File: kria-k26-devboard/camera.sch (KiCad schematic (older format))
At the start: 9 parts, among them J3 WE_68715014522, U9 PI4MSD5V9540BUEX

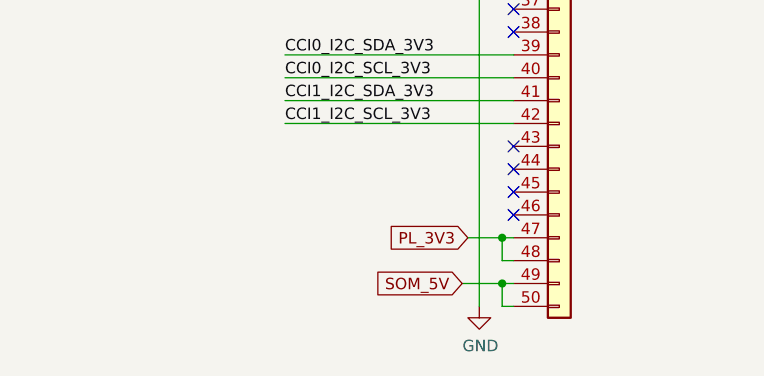
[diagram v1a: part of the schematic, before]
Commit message: Finished Power planes and overall connectivity
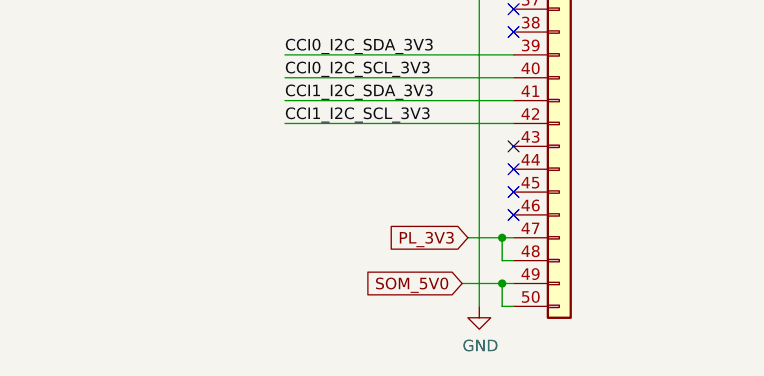
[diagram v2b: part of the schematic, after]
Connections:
- net SOM_5V renamed SOM_5V0
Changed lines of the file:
@@
 NoConn ~ 8500 5100
 Text GLabel 8275 5700 0    50   Input ~ 0
-SOM_5V
+SOM_5V0
 Wire Wire Line
 	8500 5800 8450 5800

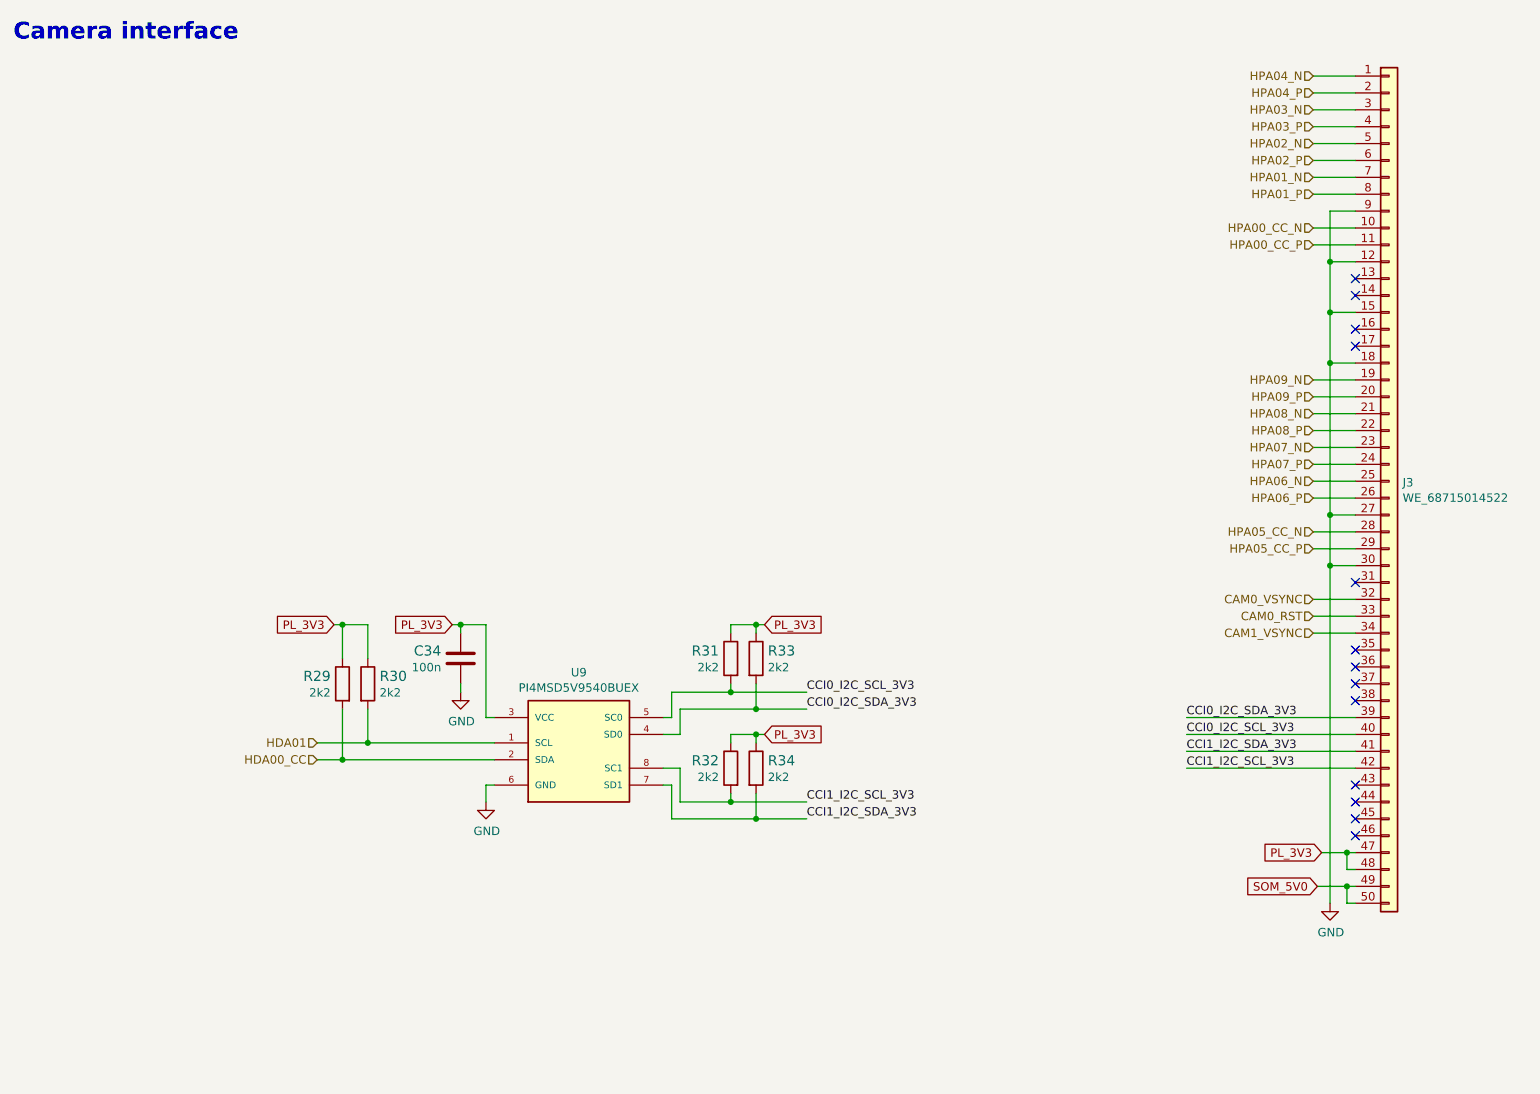
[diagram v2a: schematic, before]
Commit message: Applied schematic review suggestions
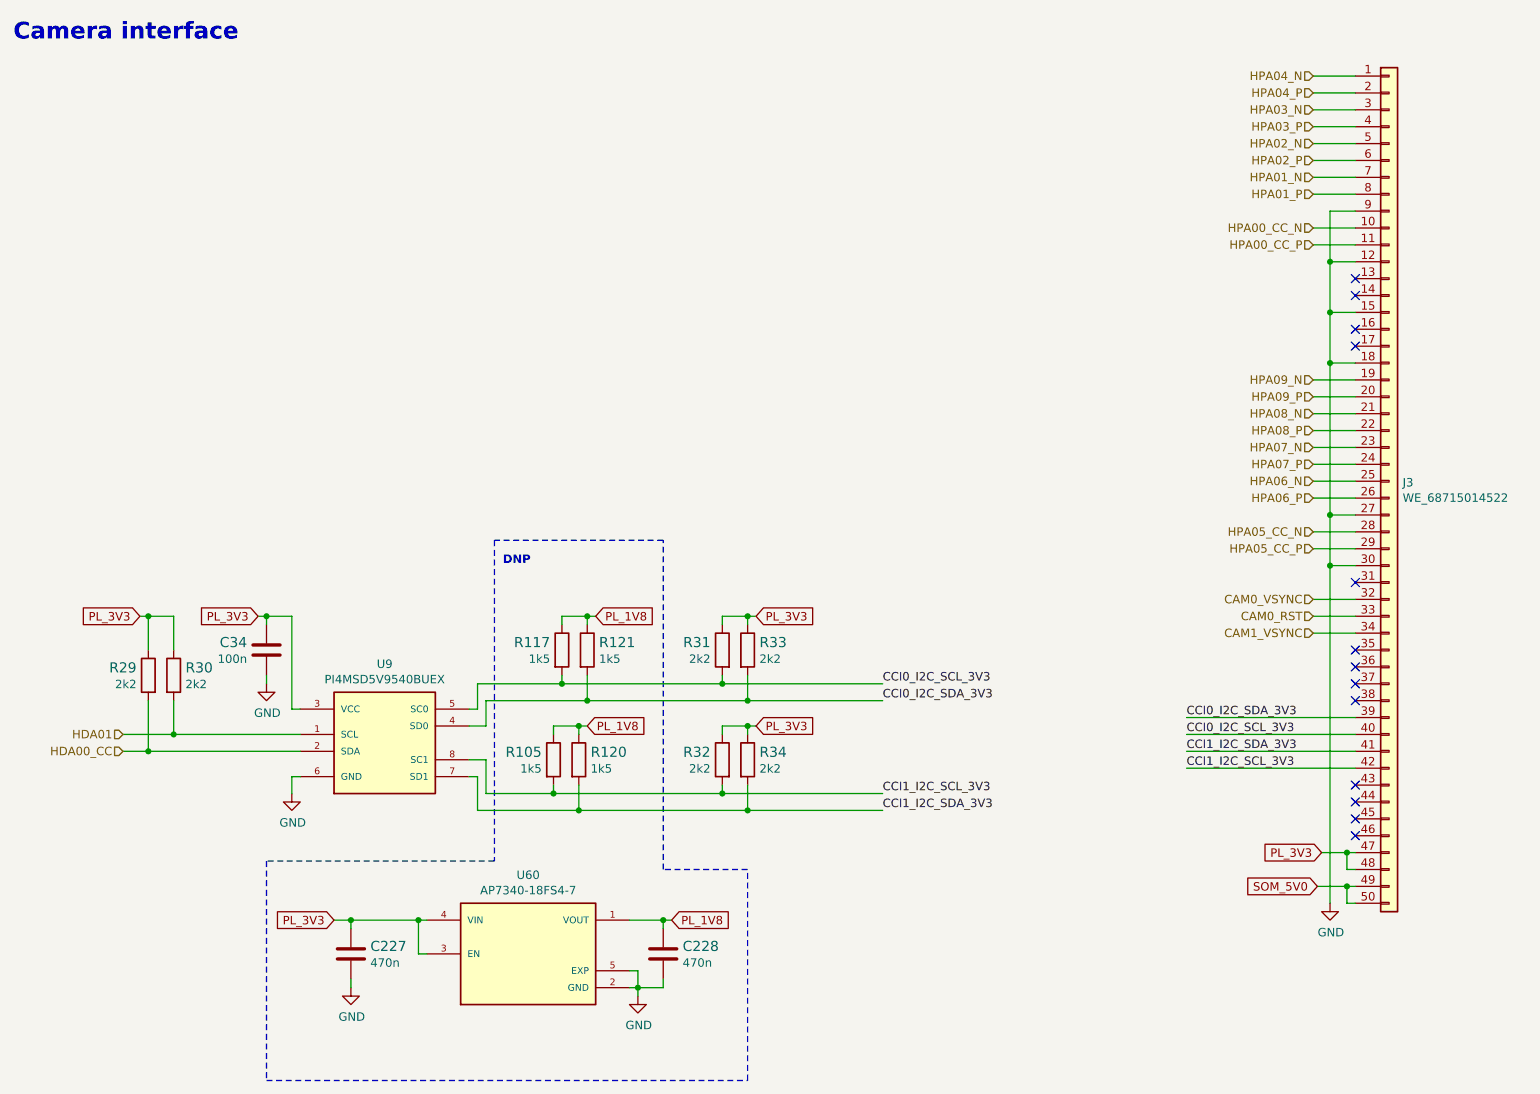
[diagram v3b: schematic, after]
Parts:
- added C227, C228: C_470n_0402, antmicro-footprints:0402-cap, symbol antmicroCapacitors0402:C_470n_0402
- added R105, R117, R120, R121: R_1k5_0402, antmicro-footprints:0402-res, symbol antmicroResistors0402:R_1k5_0402
- added U60: AP7340-18FS4-7, antmicro-footprints:XDFN4, symbol antmicroPMICVoltageRegulatorsLinear:AP7340-18FS4-7
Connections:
- net CCI0_I2C_SCL_3V3: now also R117.2
- net CCI0_I2C_SDA_3V3: now also R121.2
- net CCI1_I2C_SCL_3V3: now also R105.2
- net CCI1_I2C_SDA_3V3: now also R120.2
- net GND: now also C227.2, C228.2, U60.2 (GND), U60.5 (EXP)
- net PL_3V3: now also C227.1, U60.3 (EN), U60.4 (VIN)
- new net PL_1V8: C228.1, R105.1, R117.1, R120.1, R121.1, U60.1 (VOUT)
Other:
- note added: "DNP"
- moved on the sheet: C34, R29, R30, R31, R32, R33, R34, U9
